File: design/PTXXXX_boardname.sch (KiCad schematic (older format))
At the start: 0 parts

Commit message: added 4off M3 mounting holes as default added useful descriptive text as default updated library refs to latest
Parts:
- added H1, H2, H3, H4: M3 Hole, MountingHole:MountingHole_3.5mm_Pad_Via, symbol Mechanical:MountingHole_Pad
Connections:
- net labels added: GND
- wire segments 0 -> 10
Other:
- note added: "Descriptive text about a circuit block / interface."
- note added: "Route as matched length 100R differential pairs"
- note added: "Title"
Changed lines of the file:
@@
 Comment4 ""
 $EndDescr
+$Comp
+L Mechanical:MountingHole_Pad H1
+U 1 1 5EAEED3F
+P 1450 6950
+F 0 "H1" H 1550 6999 50  0000 L CNN
+F 1 "M3 Hole" H 1550 6908 50  0000 L CNN
+F 2 "MountingHole:MountingHole_3.5mm_Pad_Via" H 1450 6950 50  0001 C CNN
+F 3 "~" H 1450 6950 50  0001 C CNN
+F 4 "M3 Mounting Hole" H 1450 6950 50  0001 C CNN "Description"
+F 5 "N/A" H 1450 6950 50  0001 C CNN "Manufacturer1"
+F 6 "N/A" H 1450 6950 50  0001 C CNN "MPN1"
+F 7 "DNF" H 1450 6950 50  0001 C CNN "FitPart"
+	1    1450 6950
+	1    0    0    -1
+$EndComp
+$Comp
+L power:GND #PWR01
+U 1 1 5EAEF4ED
+P 1450 7250
+F 0 "#PWR01" H 1450 7000 50  0001 C CNN
+F 1 "GND" H 1455 7077 50  0000 C CNN
+F 2 "" H 1450 7250 50  0001 C CNN
+F 3 "" H 1450 7250 50  0001 C CNN
+	1    1450 7250
+	1    0    0    -1
+$EndComp
+Wire Wire Line
+	1450 7050 1450 7150
+$Comp
+L Mechanical:MountingHole_Pad H2
+U 1 1 5EAEFEA5
+P 1950 6950
+F 0 "H2" H 2050 6999 50  0000 L CNN
+F 1 "M3 Hole" H 2050 6908 50  0000 L CNN
+F 2 "MountingHole:MountingHole_3.5mm_Pad_Via" H 1950 6950 50  0001 C CNN
+F 3 "~" H 1950 6950 50  0001 C CNN
+F 4 "M3 Mounting Hole" H 1950 6950 50  0001 C CNN "Description"
+F 5 "N/A" H 1950 6950 50  0001 C CNN "Manufacturer1"
+F 6 "N/A" H 1950 6950 50  0001 C CNN "MPN1"
+F 7 "DNF" H 1950 6950 50  0001 C CNN "FitPart"
+	1    1950 6950
+	1    0    0    -1
+$EndComp
+$Comp
+L Mechanical:MountingHole_Pad H3
+U 1 1 5EAF0AC1
+P 2450 6950
+F 0 "H3" H 2550 6999 50  0000 L CNN
+F 1 "M3 Hole" H 2550 6908 50  0000 L CNN
+F 2 "MountingHole:MountingHole_3.5mm_Pad_Via" H 2450 6950 50  0001 C CNN
+F 3 "~" H 2450 6950 50  0001 C CNN
+F 4 "M3 Mounting Hole" H 2450 6950 50  0001 C CNN "Description"
+F 5 "N/A" H 2450 6950 50  0001 C CNN "Manufacturer1"
+F 6 "N/A" H 2450 6950 50  0001 C CNN "MPN1"
+F 7 "DNF" H 2450 6950 50  0001 C CNN "FitPart"
+	1    2450 6950
+	1    0    0    -1
+$EndComp
+$Comp
+L Mechanical:MountingHole_Pad H4
+U 1 1 5EAF13ED
+P 2950 6950
+F 0 "H4" H 3050 6999 50  0000 L CNN
+F 1 "M3 Hole" H 3050 6908 50  0000 L CNN
+F 2 "MountingHole:MountingHole_3.5mm_Pad_Via" H 2950 6950 50  0001 C CNN
+F 3 "~" H 2950 6950 50  0001 C CNN
+F 4 "M3 Mounting Hole" H 2950 6950 50  0001 C CNN "Description"
+F 5 "N/A" H 2950 6950 50  0001 C CNN "Manufacturer1"
+F 6 "N/A" H 2950 6950 50  0001 C CNN "MPN1"
+F 7 "DNF" H 2950 6950 50  0001 C CNN "FitPart"
+	1    2950 6950
+	1    0    0    -1
+$EndComp
+Wire Wire Line
+	1450 7150 1950 7150
+Wire Wire Line
+	1950 7150 1950 7050
+Connection ~ 1450 7150
+Wire Wire Line
+	1450 7150 1450 7250
+Wire Wire Line
+	1950 7150 2450 7150
+Wire Wire Line
+	2450 7150 2450 7050
+Connection ~ 1950 7150
+Wire Wire Line
+	2450 7150 2950 7150
+Wire Wire Line
+	2950 7150 2950 7050
+Connection ~ 2450 7150
+Text Notes 2050 2450 0    79   ~ 16
+Title
+Text Notes 2050 2600 0    59   ~ 0
+Descriptive text about a circuit block / interface.
+Wire Wire Line
+	6350 7500 6600 7500
+Wire Wire Line
+	6350 7400 6600 7400
+Wire Notes Line
+	6450 7350 6450 7550
+Wire Notes Line
+	6450 7550 6500 7550
+Wire Notes Line
+	6500 7550 6500 7350
+Wire Notes Line
+	6500 7350 6450 7350
+Text Notes 4000 7500 0    59   ~ 0
+Route as matched length 100R differential pairs
 $EndSCHEMATC

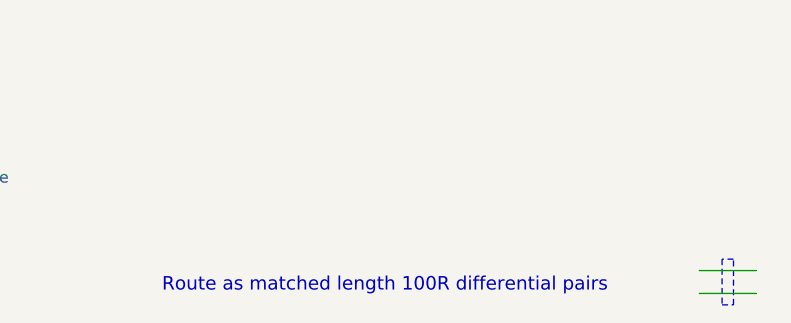
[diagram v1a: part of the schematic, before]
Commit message: changed differential pair description to use 'Z' rather than 'R' for impedance KiCAD removed cache library on its own updated library ref to latest
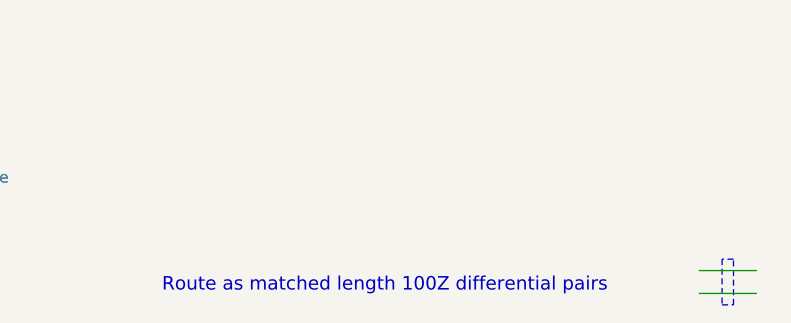
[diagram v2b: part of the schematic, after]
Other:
- note added: "Route as matched length 100Z differential pairs"
- note removed: "Route as matched length 100R differential pairs"
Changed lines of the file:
@@
 EESchema Schematic File Version 4
-LIBS:PTXXXX_boardname-cache
 EELAYER 30 0
 EELAYER END
@@
 	6500 7350 6450 7350
 Text Notes 4000 7500 0    59   ~ 0
-Route as matched length 100R differential pairs
+Route as matched length 100Z differential pairs
 $EndSCHEMATC

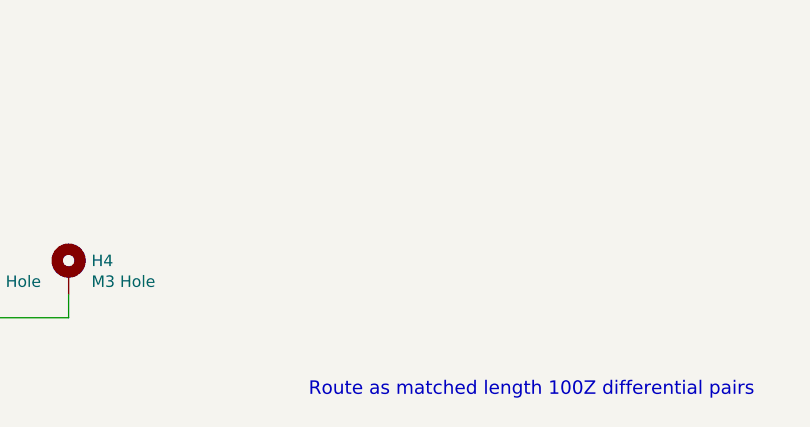
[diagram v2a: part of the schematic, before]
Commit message: added LOGO1 for optimised silkscreen logo corrected titleblock reference, was still kbconsulting re-imported to PCB and placed optimised logo deleted silkscreen optimised text
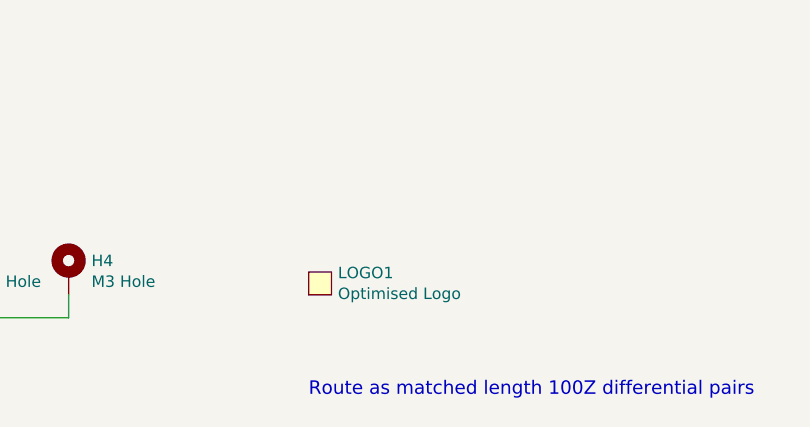
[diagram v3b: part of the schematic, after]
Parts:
- added LOGO1: Optimised Logo, _kb_miscellaneous:PCB_Silk_Logo_Optimised, symbol _kb_miscellaneous:Logo
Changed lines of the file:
@@
 Text Notes 4000 7500 0    59   ~ 0
 Route as matched length 100Z differential pairs
+$Comp
+L _kb_miscellaneous:Logo LOGO1
+U 1 1 60625BFA
+P 4050 7000
+F 0 "LOGO1" H 4128 7046 50  0000 L CNN
+F 1 "Optimised Logo" H 4128 6955 50  0000 L CNN
+F 2 "_kb_miscellaneous:PCB_Silk_Logo_Optimised" H 3905 7000 50  0001 C CNN
+F 3 "${KIPRJMOD}\\optimised_kicad-libraries\\datasheets\\miscellaneous\\" H 3905 7000 50  0001 C CNN
+F 4 "PCB Logo Virtual Part" H 3950 7050 50  0001 C CNN "Description"
+F 5 "N/A" H 3950 7050 50  0001 C CNN "Manufacturer1"
+F 6 "N/A" H 3950 7050 50  0001 C CNN "MPN1"
+F 7 " " H 3950 7050 50  0001 C CNN "Manufacturer2"
+F 8 " " H 3950 7050 50  0001 C CNN "MPN2"
+F 9 " " H 3950 7050 50  0001 C CNN "Vendor1"
+F 10 " " H 3950 7050 50  0001 C CNN "SKU1"
+F 11 " " H 3950 7050 50  0001 C CNN "Vendor2"
+F 12 " " H 3950 7050 50  0001 C CNN "SKU2"
+F 13 "DNF" H 3950 7050 50  0001 C CNN "FitPart"
+	1    4050 7000
+	1    0    0    -1
+$EndComp
 $EndSCHEMATC
